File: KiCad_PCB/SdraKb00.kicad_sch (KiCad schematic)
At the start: 75 parts, among them J1 AVR-ISP-6, SW00 SW_Push_45deg, SW01 SW_Push_45deg, SW02 SW_Push_45deg, SW03 RotaryEncoder_Switch, SW10 SW_Push_45deg, SW11 SW_Push_45deg, SW12 SW_Push_45deg, SW13 SW_Push_45deg, SW20 SW_Push_45deg, SW21 SW_Push_45deg, SW22 SW_Push_45deg, SW23 SW_Push_45deg, U1 ATmega32U4-A, U2 PRTR5V0U2X, Y1 16MHz

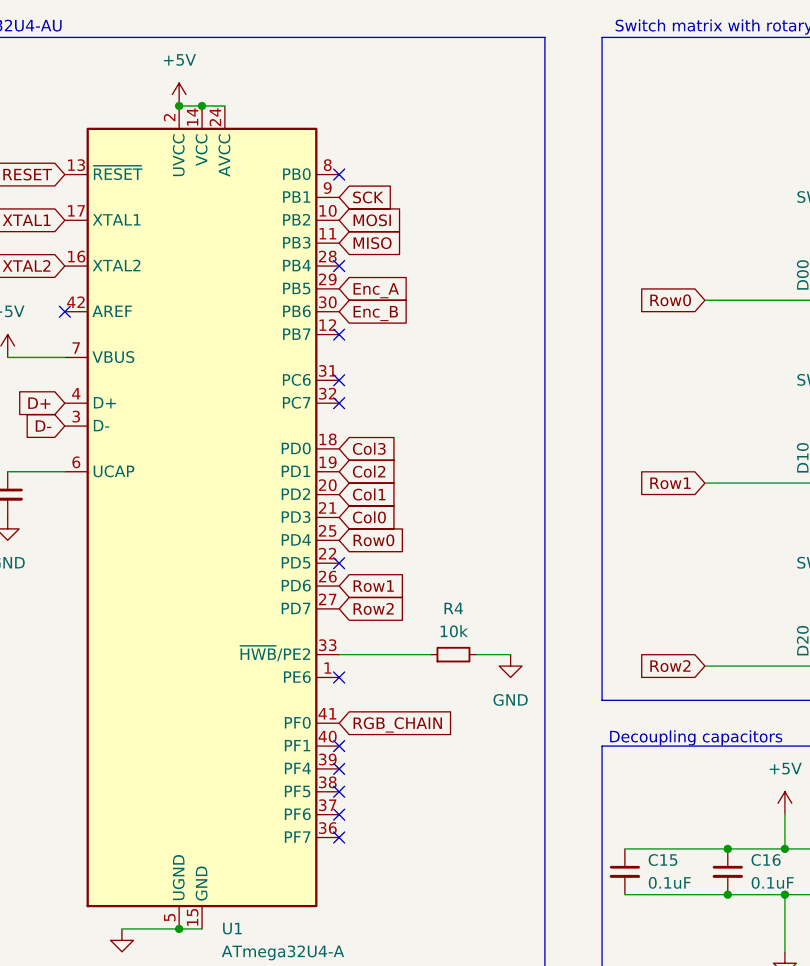
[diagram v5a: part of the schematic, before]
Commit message: Finish routing power.
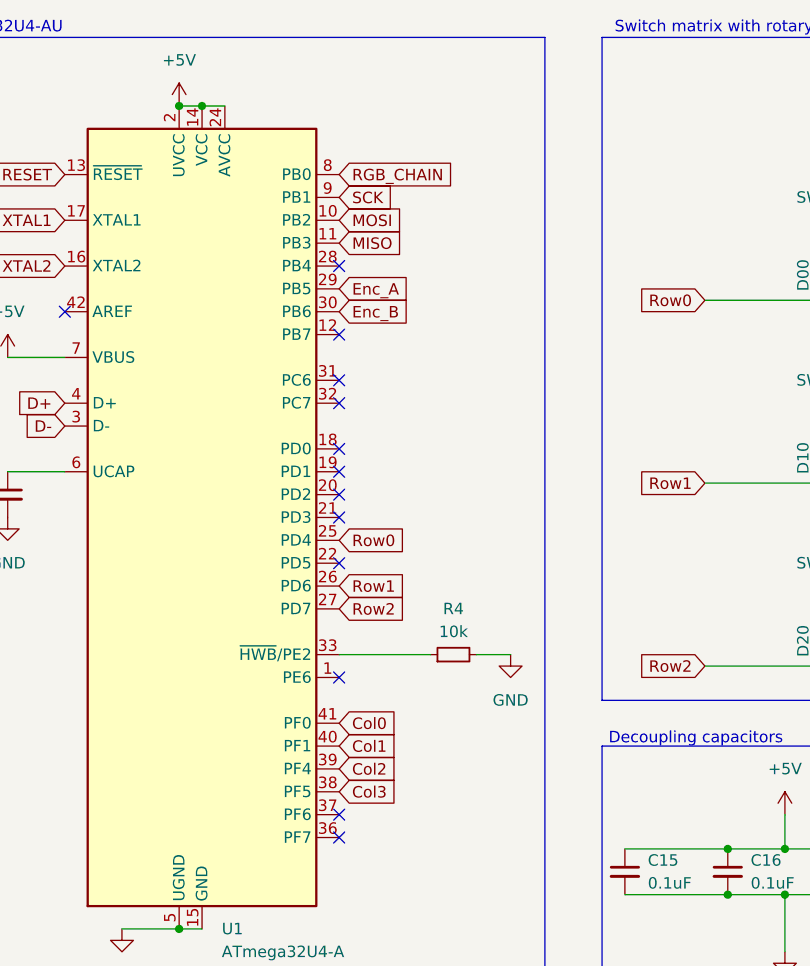
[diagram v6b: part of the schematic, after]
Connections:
- net Col0: now also U1.41 (PF0); no longer U1.21 (PD3)
- net Col1: now also U1.40 (PF1); no longer U1.20 (PD2)
- net Col2: now also U1.39 (PF4); no longer U1.19 (PD1)
- net Col3: now also U1.38 (PF5); no longer U1.18 (PD0)
- net RGB_CHAIN: now also U1.8 (PB0); no longer U1.41 (PF0)
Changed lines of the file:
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@@
-	)
-	(no_connect
-		(at 68.58 102.87)
 	)
 	(no_connect
@@
 	)
 	(no_connect
-		(at 68.58 105.41)
-	)
-	(no_connect
-		(at 68.58 36.83)
-	)
-	(no_connect
-		(at 68.58 100.33)
+		(at 68.58 74.93)
 	)
 	(no_connect
@@
 	)
 	(no_connect
+		(at 68.58 69.85)
+	)
+	(no_connect
 		(at 68.58 59.69)
 	)
@@
 	)
 	(no_connect
+		(at 68.58 67.31)
+	)
+	(no_connect
 		(at 68.58 107.95)
 	)
@@
 	(no_connect
 		(at 68.58 80.01)
+	)
+	(no_connect
+		(at 68.58 72.39)
 	)
 	(no_connect
@@
 	(global_label "Col2"
 		(shape input)
-		(at 68.58 69.85 0)
-		(fields_autoplaced yes)
-		(effects
-			(font
-				(size 1.27 1.27)
-			)
-			(justify left)
-		)
-		(property "Intersheetrefs" "${INTERSHEET_REFS}"
-			(at 75.8589 69.85 0)
+		(at 68.58 102.87 0)
+		(fields_autoplaced yes)
+		(effects
+			(font
+				(size 1.27 1.27)
+			)
+			(justify left)
+		)
+		(property "Intersheetrefs" "${INTERSHEET_REFS}"
+			(at 75.8589 102.87 0)
 			(effects
 				(font
@@
 	(global_label "Col1"
 		(shape input)
-		(at 68.58 72.39 0)
-		(fields_autoplaced yes)
-		(effects
-			(font
-				(size 1.27 1.27)
-			)
-			(justify left)
-		)
-		(property "Intersheetrefs" "${INTERSHEET_REFS}"
-			(at 75.8589 72.39 0)
+		(at 68.58 100.33 0)
+		(fields_autoplaced yes)
+		(effects
+			(font
+				(size 1.27 1.27)
+			)
+			(justify left)
+		)
+		(property "Intersheetrefs" "${INTERSHEET_REFS}"
+			(at 75.8589 100.33 0)
 			(effects
 				(font
@@
 	(global_label "Col0"
 		(shape input)
-		(at 68.58 74.93 0)
-		(fields_autoplaced yes)
-		(effects
-			(font
-				(size 1.27 1.27)
-			)
-			(justify left)
-		)
-		(property "Intersheetrefs" "${INTERSHEET_REFS}"
-			(at 75.8589 74.93 0)
+		(at 68.58 97.79 0)
+		(fields_autoplaced yes)
+		(effects
+			(font
+				(size 1.27 1.27)
+			)
+			(justify left)
+		)
+		(property "Intersheetrefs" "${INTERSHEET_REFS}"
+			(at 75.8589 97.79 0)
 			(effects
 				(font
@@
 	(global_label "Col3"
 		(shape input)
-		(at 68.58 67.31 0)
-		(fields_autoplaced yes)
-		(effects
-			(font
-				(size 1.27 1.27)
-			)
-			(justify left)
-		)
-		(property "Intersheetrefs" "${INTERSHEET_REFS}"
-			(at 75.8589 67.31 0)
+		(at 68.58 105.41 0)
+		(fields_autoplaced yes)
+		(effects
+			(font
+				(size 1.27 1.27)
+			)
+			(justify left)
+		)
+		(property "Intersheetrefs" "${INTERSHEET_REFS}"
+			(at 75.8589 105.41 0)
 			(effects
 				(font
@@
 	(global_label "RGB_CHAIN"
 		(shape input)
-		(at 68.58 97.79 0)
-		(fields_autoplaced yes)
-		(effects
-			(font
-				(size 1.27 1.27)
-			)
-			(justify left)
-		)
-		(property "Intersheetrefs" "${INTERSHEET_REFS}"
-			(at 81.9672 97.79 0)
-			(effects
-				(font
+		(at 68.58 36.83 0)
+		(fields_autoplaced yes)
+		(effects
+			(font
+				(size 1.27 1.27)
+			)
+			(justify left)
+		)
+		(property "Intersheetrefs" "${INTERSHEET_REFS}"
+			(at 81.9672 36.83 0)
+			(effects
+				(font
